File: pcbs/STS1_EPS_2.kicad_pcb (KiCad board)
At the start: 4 copper layers, 81 x 85 mm, 127 parts, among them J1 Inter-EPS, J2 Panel X+, J3 Battery Pack, J4 Panel X-, J5 Panel Y+, J6 Panel Y-, J7 Panel Z+, Q1 SI7135DP-T1-GE3, Q2 2N7002, Q3 SI7135DP-T1-GE3, Q4 2N7002, Q5 SI7135DP-T1-GE3, U1 LTC4020EUHFPBF, U10 MAX11632EEGT, U11 TMCS1101A3B-Q1, U12 BD50GA5WEFJ, U13 TMCS1101A3B-Q1, U14 LM334M, U15 LM334M, U16 LM334M, U17 LM334M, U18 LM334M, U19 TMCS1101A3B-Q1, U2 SI7272DP-T1-GE3, U20 TMCS1101A3B-Q1, U21 TMCS1101A3B-Q1, U22 TMCS1101A3B-Q1, U23 TMCS1101A3B-Q1, U24 TMCS1101A3B-Q1, U25 TMCS1101A3B-Q1, U26 TMCS1101A3B-Q1, U27 TPS2420RSAT, U3 SI7272DP-T1-GE3, U4 BQ29209DRBT, U5 MAX11632EEGT, U6 MAX11632EEGT, U7 MAX11632EEGT, U8 MAX11632EEGT, U9 MAX11632EEGT

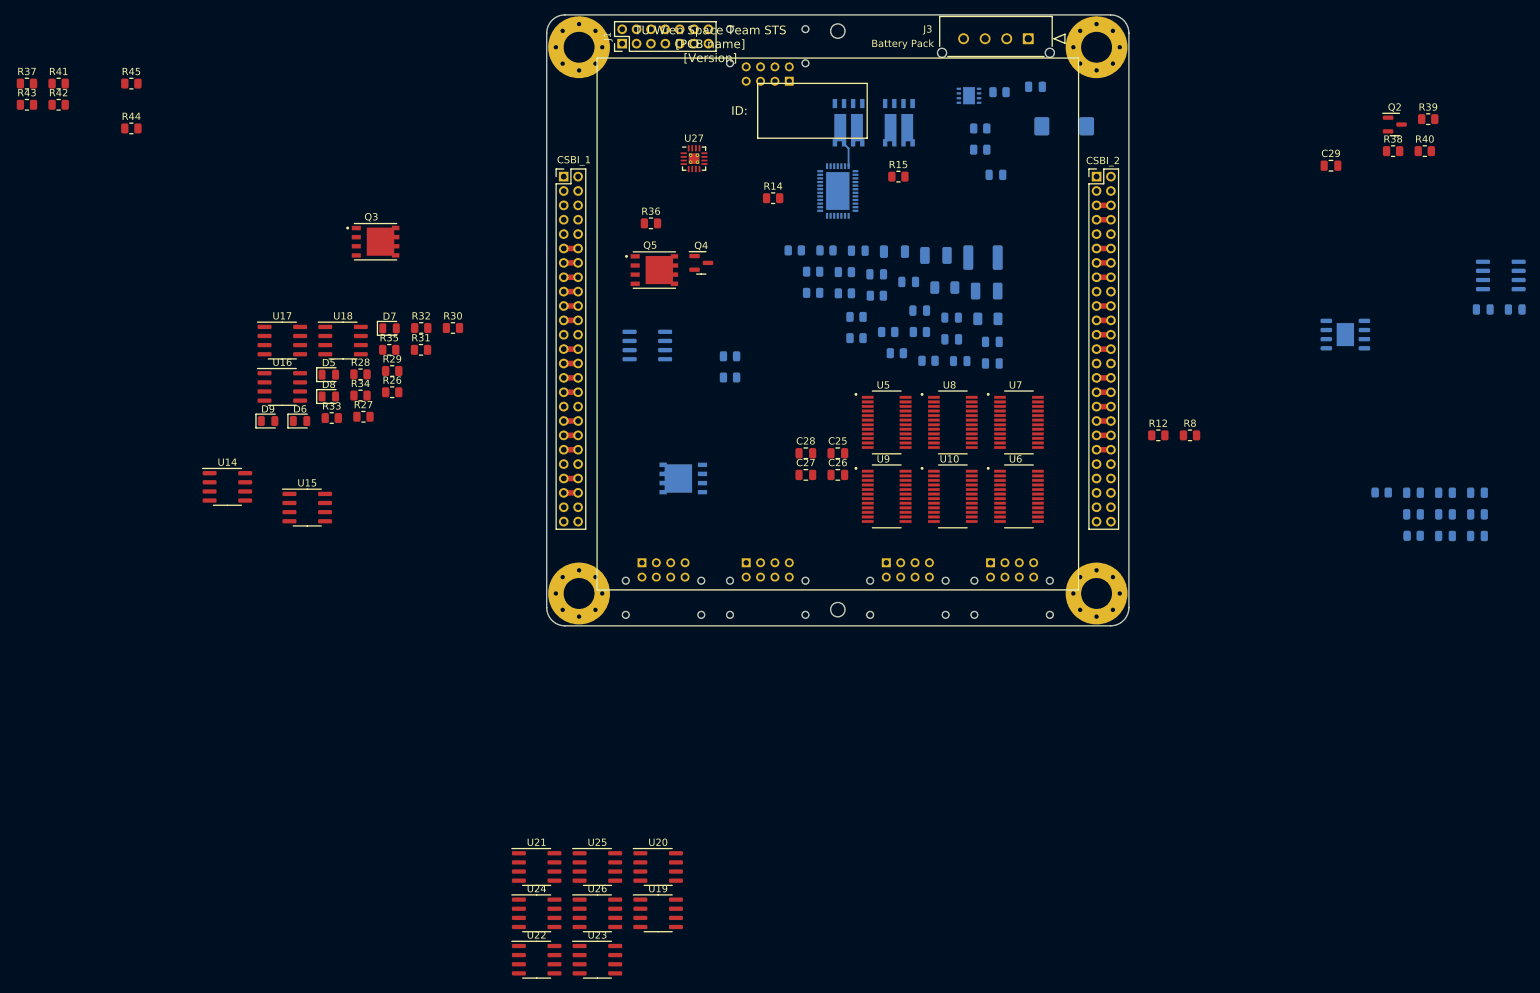
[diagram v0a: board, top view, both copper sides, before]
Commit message: Worked on STS1_EPS_1 and began work on STS1_EPS_2.
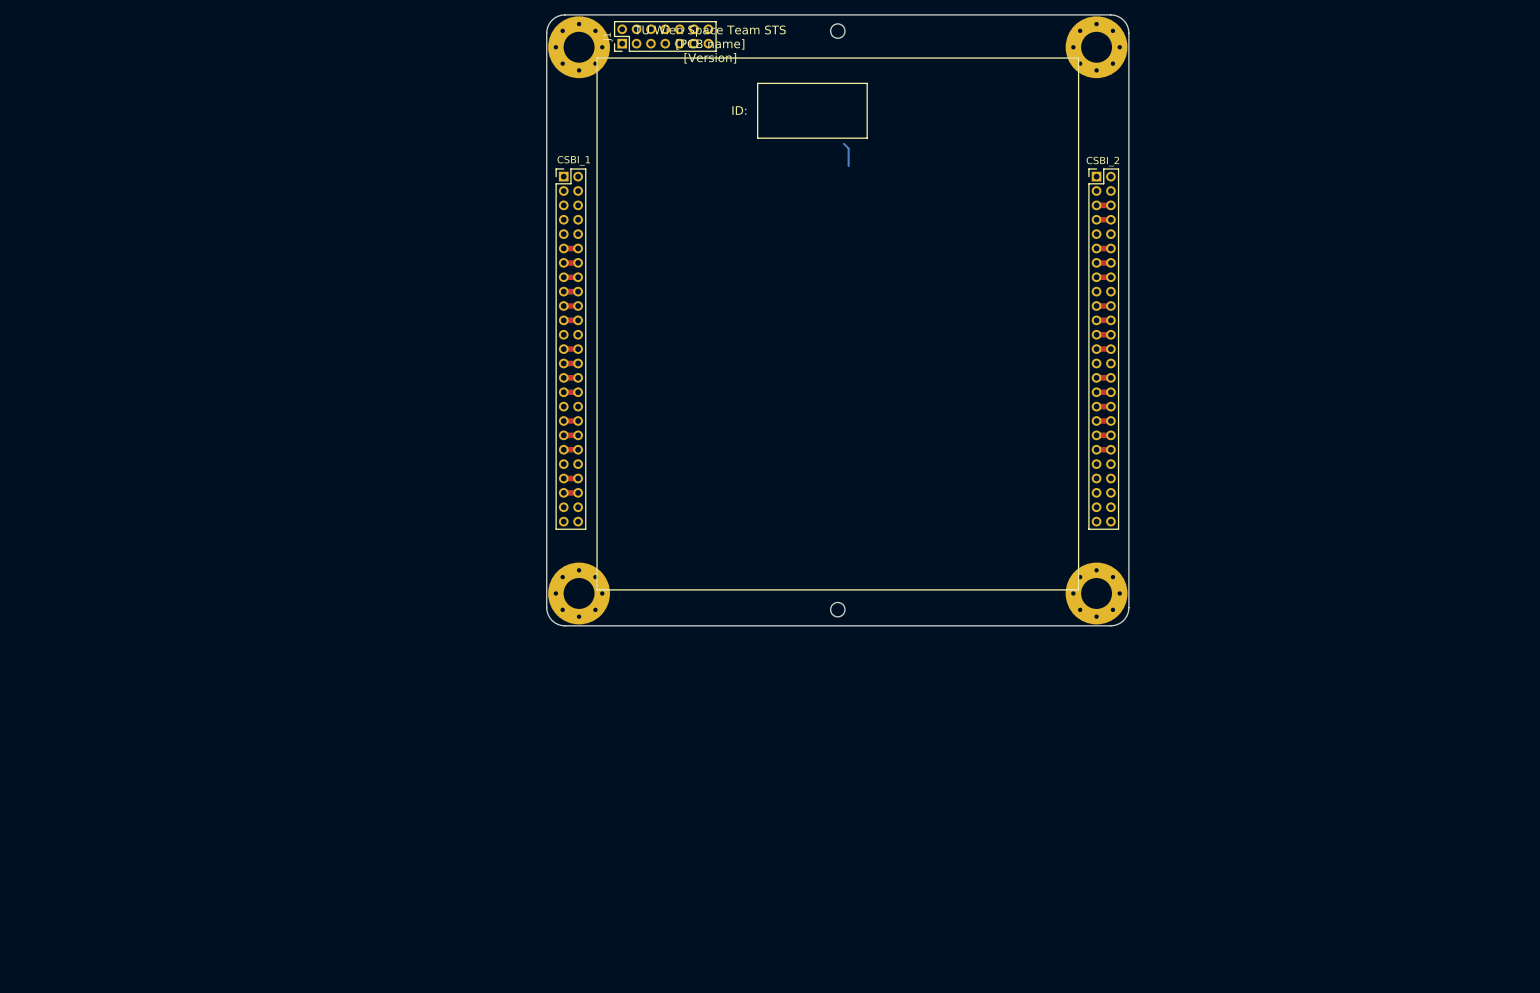
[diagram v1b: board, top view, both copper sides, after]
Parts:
- removed C1: 50u, Capacitor_Tantalum_SMD:CP_EIA-3528-12_Kemet-T
- removed C10, C9: 680p, Capacitor_SMD:C_0805_2012Metric
- removed C11: 330n, Capacitor_SMD:C_0805_2012Metric
- removed C12, C13, C17, C18, C19, C20, C21, C22, C23, C24, C25, C26, C27, C28: 100n, Capacitor_SMD:C_0805_2012Metric
- removed C14: 330u, Capacitor_Tantalum_SMD:CP_EIA-7343-43_Kemet-X
- removed C15, C16, C29: 1u, Capacitor_SMD:C_0805_2012Metric
- removed C2, C3: 1µ, Capacitor_SMD:C_0805_2012Metric
- removed C5: 220µ, Capacitor_Tantalum_SMD:CP_EIA-3528-12_Kemet-T
- removed C6: 2µ2, Capacitor_SMD:C_0805_2012Metric
- removed C7: 10µ, Capacitor_SMD:C_0805_2012Metric
- removed C8: 200n, Capacitor_SMD:C_1812_4532Metric
- removed D1, D2: SD1206T040S1R0, Diode_SMD:D_1206_3216Metric
- removed D3, D4: LED, LED_SMD:LED_0805_2012Metric
- removed D5, D6, D7, D8, D9: TS4148 RYG, Diode_SMD:D_0805_2012Metric
- removed J2: Panel X+, STS_Connector:M8085108
- removed J3: Battery Pack, STS_Connector:436500415
- removed J4: Panel X-, STS_Connector:M8085108
- removed J5: Panel Y+, STS_Connector:M8085108
- removed J6: Panel Y-, STS_Connector:M8085108
- removed J7: Panel Z+, STS_Connector:M8085108
- removed Q1, Q3, Q5: SI7135DP-T1-GE3, STS_Package_SO:POWERPAK_SO8_single
- removed Q2, Q4: 2N7002, Package_TO_SOT_SMD:SOT-23
- removed R1: 135k, Resistor_SMD:R_0805_2012Metric
- removed R10, R11: 1k, Resistor_SMD:R_0805_2012Metric
- removed R12, R2, R25, R37, R4, R41, R6, R8: 100k, Resistor_SMD:R_0805_2012Metric
- removed R13: 53k6, Resistor_SMD:R_0805_2012Metric
- removed R14, R15: 30m, Resistor_SMD:R_0805_2012Metric
- removed R16, R17, R36: R, Resistor_SMD:R_0805_2012Metric
- removed R18, R19, R21: 100, Resistor_SMD:R_0805_2012Metric
- removed R20: 17m, Resistor_SMD:R_1206_3216Metric
- removed R22, R23: 140, Resistor_SMD:R_0805_2012Metric
- removed R24: 87k5, Resistor_SMD:R_0805_2012Metric
- removed R26, R28, R30, R32, R34: 332, Resistor_SMD:R_0805_2012Metric
- removed R27, R29, R31, R33, R35: 3320, Resistor_SMD:R_0805_2012Metric
- removed R3: 180k, Resistor_SMD:R_0805_2012Metric
- removed R38: 40k2, Resistor_SMD:R_0805_2012Metric
- removed R39: 64k, Resistor_SMD:R_0805_2012Metric
- removed R40: 31k5, Resistor_SMD:R_0805_2012Metric
- removed R42, R43, R44, R45: 0, Resistor_SMD:R_0805_2012Metric
- removed R5: 31k, Resistor_SMD:R_0805_2012Metric
- removed R7: 500k, Resistor_SMD:R_0805_2012Metric
- removed R9: 166k, Resistor_SMD:R_0805_2012Metric
- removed U1: LTC4020EUHFPBF, STS_Package_DFN_QFN:AD_QFN-38_UHF
- removed U10, U5, U6, U7, U8, U9: MAX11632EEGT, STS_Package_QSOP:MAX_QSOP24
- removed U11, U13, U19, U20, U21, U22, U23, U24, U25, U26: TMCS1101A3B-Q1, Package_SO:SOIC-8_3.9x4.9mm_P1.27mm
- removed U12: BD50GA5WEFJ, Package_SO:HTSOP-8-1EP_3.9x4.9mm_P1.27mm_EP2.4x3.2mm
- removed U14, U15, U16, U17, U18: LM334M, Package_SO:SOIC-8_3.9x4.9mm_P1.27mm
- removed U2, U3: SI7272DP-T1-GE3, STS_Package_SO:POWERPAK_SO8
- removed U27: TPS2420RSAT, Package_DFN_QFN:VQFN-16-1EP_3x3mm_P0.5mm_EP1.45x1.45mm_ThermalVias
- removed U4: BQ29209DRBT, STS_Package_VSON:TI_VSON8
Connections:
- net GNDREF renamed /DS2_H
- J1 pad 11: GND -> /DS2_L
- J1 pad 9: GND -> /DS2_L
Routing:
- net /Battery Charge Controller/SW1: track 3.36 -> 0.00 mm
- net (no net): track 0.00 -> 3.36 mm
- added copper zone on In1.Cu, net /DS2_L
- removed copper zone on In1.Cu, net GND

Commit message: Finished first revision of schematic.
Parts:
- added C1: 100n, Capacitor_SMD:C_0805_2012Metric, F.Cu at (87.1, 68.8)
- added C2: 100n, Capacitor_SMD:C_0805_2012Metric, F.Cu at (223.1, 103.3)
- added C29: 1u, Capacitor_SMD:C_0805_2012Metric, F.Cu at (30.8, 111.2)
- added C3: 100n, Capacitor_SMD:C_0805_2012Metric, F.Cu at (218.7, 103.3)
- added C4: 100n, Capacitor_SMD:C_0805_2012Metric, F.Cu at (227.6, 103.3)
- added C5: 100n, Capacitor_SMD:C_0805_2012Metric, F.Cu at (238.2, 90.0)
- added F1: Fuse, Resistor_SMD:R_1206_3216Metric, F.Cu at (243.1, 83.8)
- added J2: DS1, STS_Connector:M808420245, F.Cu at (129.1, 119.4)
- added J3: DS2, STS_Connector:M808420245, F.Cu at (139.1, 119.4)
- added J4: DS3, STS_Connector:M808420245, F.Cu at (149.1, 119.4)
- added J5: DS4, STS_Connector:M808420245, F.Cu at (159.1, 119.4)
- added J6: RBF, STS_Connector:M808420245, F.Cu at (169.1, 119.4)
- added J7: Antenna Deployment, STS_Connector:M80-85104YY, F.Cu at (179.1, 54.8)
- added J8: UCI, STS_Connector:M80-85110YY, F.Cu at (155.6, 54.8)
- added Q1: 2N7002, Package_TO_SOT_SMD:SOT-23, F.Cu at (228.7, 99.6)
- added Q10: 2N7002, Package_TO_SOT_SMD:SOT-23, F.Cu at (218.9, 95.1)
- added Q11: SI7272DP-T1-GE3, STS_Package_SO:POWERPAK_SO8, F.Cu at (251.5, 100.4)
- added Q12: SI7272DP-T1-GE3, STS_Package_SO:POWERPAK_SO8, F.Cu at (251.5, 92.4)
- added Q13: 2N7002, Package_TO_SOT_SMD:SOT-23, F.Cu at (218.9, 90.7)
- added Q14: 2N7002, Package_TO_SOT_SMD:SOT-23, F.Cu at (218.9, 99.6)
- added Q15: 2N7002, Package_TO_SOT_SMD:SOT-23, F.Cu at (233.6, 90.7)
- added Q16: BSS83P, Package_TO_SOT_SMD:SOT-23, F.Cu at (233.6, 95.1)
- added Q17: 2N7002, Package_TO_SOT_SMD:SOT-23, F.Cu at (223.8, 95.1)
- added Q18: 2N7002, Package_TO_SOT_SMD:SOT-23, F.Cu at (248.2, 110.9)
- added Q19: SI7272DP-T1-GE3, STS_Package_SO:POWERPAK_SO8, F.Cu at (246.6, 75.3)
- added Q2: SI7135DP-T1-GE3, STS_Package_SO:POWERPAK_SO8_single, F.Cu at (39.6, 104.3)
- added Q20: 2N7002, Package_TO_SOT_SMD:SOT-23, F.Cu at (253.0, 110.9)
- added Q21: 2N7002, Package_TO_SOT_SMD:SOT-23, F.Cu at (248.2, 115.3)
- added Q3: SI7135DP-T1-GE3, STS_Package_SO:POWERPAK_SO8_single, F.Cu at (33.1, 100.0)
- added Q4: SI7135DP-T1-GE3, STS_Package_SO:POWERPAK_SO8_single, F.Cu at (44.9, 99.0)
- added Q5: SI7135DP-T1-GE3, STS_Package_SO:POWERPAK_SO8_single, F.Cu at (33.1, 106.5)
- added Q6: 2N7002, Package_TO_SOT_SMD:SOT-23, F.Cu at (223.8, 90.7)
- added Q7: 2N7002, Package_TO_SOT_SMD:SOT-23, F.Cu at (223.8, 99.6)
- added Q8: BSS83P, Package_TO_SOT_SMD:SOT-23, F.Cu at (228.7, 90.7)
- added Q9: 2N7002, Package_TO_SOT_SMD:SOT-23, F.Cu at (228.7, 95.1)
- added R1: 0, Resistor_SMD:R_0805_2012Metric, F.Cu at (43.8, 108.0)
- added R10: 100k, Resistor_SMD:R_0805_2012Metric, F.Cu at (279.3, 89.9)
- added R11: 0, Resistor_SMD:R_0805_2012Metric, F.Cu at (274.9, 95.8)
- added R12: 100k, Resistor_SMD:R_0805_2012Metric, F.Cu at (256.7, 119.0)
- added R13: 100k, Resistor_SMD:R_0805_2012Metric, F.Cu at (257.2, 116.0)
- added R14: 100k, Resistor_SMD:R_0805_2012Metric, F.Cu at (262.1, 113.1)
- added R15: 100k, Resistor_SMD:R_0805_2012Metric, F.Cu at (261.6, 116.0)
- added R16: 100k, Resistor_SMD:R_0805_2012Metric, F.Cu at (257.7, 110.1)
- added R17: 1M, Resistor_SMD:R_0805_2012Metric, F.Cu at (257.7, 113.1)
- added R18: 887k, Resistor_SMD:R_0805_2012Metric, F.Cu at (252.8, 114.6)
- added R19: 127k, Resistor_SMD:R_0805_2012Metric, F.Cu at (262.1, 110.1)
- added R2: 100k, Resistor_SMD:R_0805_2012Metric, F.Cu at (232.0, 103.3)
- added R20: 127k, Resistor_SMD:R_0805_2012Metric, F.Cu at (261.1, 119.0)
- added R21: 127k, Resistor_SMD:R_0805_2012Metric, F.Cu at (247.9, 119.0)
- added R22: 187k, Resistor_SMD:R_0805_2012Metric, F.Cu at (270.2, 117.1)
- added R23: 787k, Resistor_SMD:R_0805_2012Metric, F.Cu at (275.0, 110.1)
- added R24: 10k, Resistor_SMD:R_0805_2012Metric, F.Cu at (270.2, 114.2)
- added R25: 470k, Resistor_SMD:R_0805_2012Metric, F.Cu at (243.8, 8.78)
- added R3: 100k, Resistor_SMD:R_0805_2012Metric, F.Cu at (238.2, 92.9)
- added R37: 100k, Resistor_SMD:R_0805_2012Metric, F.Cu at (39.4, 108.0)
- added R38: 40k2, Resistor_SMD:R_0805_2012Metric, F.Cu at (35.2, 111.2)
- added R39: 64k, Resistor_SMD:R_0805_2012Metric, F.Cu at (44.3, 103.5)
- added R4: 100k, Resistor_SMD:R_0805_2012Metric, F.Cu at (233.3, 98.8)
- added R40: 31k5, Resistor_SMD:R_0805_2012Metric, F.Cu at (49.6, 98.2)
- added R41: 100k, Resistor_SMD:R_0805_2012Metric, F.Cu at (39.6, 110.9)
- added R42: 0, Resistor_SMD:R_0805_2012Metric, F.Cu at (54.0, 98.2)
- added R5: 100k, Resistor_SMD:R_0805_2012Metric, F.Cu at (238.2, 95.9)
- added R6: 100k, Resistor_SMD:R_0805_2012Metric, F.Cu at (252.3, 119.0)
- added R7: 100k, Resistor_SMD:R_0805_2012Metric, F.Cu at (242.7, 89.9)
- added R8: 100k, Resistor_SMD:R_0805_2012Metric, F.Cu at (274.9, 89.9)
- added R9: 0, Resistor_SMD:R_0805_2012Metric, F.Cu at (274.9, 92.9)
- added U1: LTC6995IDCB-1, Package_DFN_QFN:DFN-6-1EP_3x2mm_P0.5mm_EP1.65x1.35mm, F.Cu at (87.5, 65.5)
- added U2: 4072, Package_SO:SOIC-14_3.9x8.7mm_P1.27mm, F.Cu at (227.1, 69.3)
- added U27: TPS2420RSAT, Package_DFN_QFN:VQFN-16-1EP_3x3mm_P0.5mm_EP1.45x1.45mm_ThermalVias, F.Cu at (39.8, 99.4)
- added U3: MIC841, Package_DFN_QFN:TDFN-6-1EP_2.5x2.5mm_P0.65mm_EP1.3x2mm, F.Cu at (163.1, 68.3)
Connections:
- net /Analog Digital Converters/COBC_SPI_1 renamed /CSBI/COBC_SPI_1
- net /Analog Digital Converters/COBC_SPI_2 renamed /CSBI/COBC_SPI_2
- net /Analog Digital Converters/COBC_SPI_3 renamed /CSBI/COBC_SPI_3
- net /Analog Digital Converters/COBC_SPI_4 renamed /CSBI/COBC_SPI_4
- net /Analog Digital Converters/COBC_SPI_5 renamed /CSBI/COBC_SPI_5
- net /Analog Digital Converters/COBC_SPI_6 renamed /CSBI/COBC_SPI_6
- net /Analog Digital Converters/EDU_SPI_1 renamed /CSBI/EDU_SPI_1
- net /Analog Digital Converters/EDU_SPI_2 renamed /CSBI/EDU_SPI_2
- net /Analog Digital Converters/EDU_SPI_3 renamed /CSBI/EDU_SPI_3
- net /Analog Digital Converters/EDU_SPI_4 renamed /CSBI/EDU_SPI_4
- net /Analog Digital Converters/EDU_SPI_5 renamed /CSBI/EDU_SPI_5
- net /Analog Digital Converters/EDU_SPI_6 renamed /CSBI/EDU_SPI_6
- net /BAT_FAULT renamed /EPS_BAT_FAULT
- net /BAT_GOOD renamed /EPS_BAT_GOOD
- net /Cubesat Bus Interface/UART_COBC_EDU_1 renamed /CSBI/UART_COBC_EDU_1
- net /Cubesat Bus Interface/UART_COBC_EDU_2 renamed /CSBI/UART_COBC_EDU_2
- net /Cubesat Bus Interface/UCI_COBC_UART_1 renamed /CSBI/UCI_COBC_UART_1
- net /Cubesat Bus Interface/UCI_COBC_UART_2 renamed /CSBI/UCI_COBC_UART_2
- CSBI_2 pad 23: unconnected-(CSBI_2-Pad23) -> /EPS_ANT_DEPLOY
- CSBI_2 pad 25: /BAT_CHARGING -> unconnected-(CSBI_2-Pad25)
- CSBI_2 pad 26: /BAT_CHARGING -> unconnected-(CSBI_2-Pad25)
- J1 pad 1: /DS1_H -> /INTERNAL_V
- J1 pad 10: /DS3_H -> /DS2_SIGNAL_1
- J1 pad 11: /DS2_L -> GND
- J1 pad 12: /DS4_L -> GND
- J1 pad 13: /DS3_H -> GND
- J1 pad 14: /DS4_L -> GND
- J1 pad 3: /DS1_L -> /INTERNAL_V
- J1 pad 5: /DS2_H -> /INTERNAL_V
- J1 pad 6: /DT_SIGNAL -> /BATT_RAW
- J1 pad 7: /DS2_H -> /INTERNAL_V
- J1 pad 8: /RBF_SIGNAL -> /VOUT_I
- J1 pad 9: /DS2_L -> /DS1_SIGNAL_1
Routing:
- net unconnected-(CSBI_2-Pad25): track 0.00 -> 2.00 mm
- net unconnected-(CSBI_2-Pad24): track 2.00 -> 0.00 mm
- net /EPS_ANT_DEPLOY: track 0.00 -> 2.00 mm
- net /BAT_CHARGING: track 2.00 -> 0.00 mm
- added copper zone on In1.Cu, net GND
- removed copper zone on In1.Cu, net /DS2_L
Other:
- outline, holes or cut-outs redrawn
- board text added: "TU Wien Space Team STS STS1_EPS_2 1.0"
- board text removed: "TU Wien Space Team STS [PCB name] [Version]"

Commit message: Worked on STS1_EPS_2 layout.
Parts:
- moved U3 45.4 mm to (208.4, 65.8)
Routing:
- net (no net): track 3.36 -> 0.00 mm

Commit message: EPS_2 Layout nearly finished, alot DRC Errors
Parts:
- moved Q3 138.4 mm to (169.3, 75.5), turned to 90 degrees
- moved R11 137.2 mm to (138.9, 77.4), turned to 90 degrees
- moved R10 135.7 mm to (143.9, 80.6)
- moved R37 134.0 mm to (170.6, 80.6)
- moved Q5 131.0 mm to (160.4, 75.5), turned to 90 degrees
- moved R9 128.0 mm to (147.7, 77.4), turned to 90 degrees
- moved R23 127.5 mm to (157.9, 59.5), turned to 90 degrees
- moved R6 126.4 mm to (126.2, 111.6), turned to 90 degrees
- moved R41 125.8 mm to (161.7, 80.6)
- moved R24 123.2 mm to (157.9, 63.3), turned to 90 degrees
- moved R22 122.9 mm to (157.9, 67.2), turned to 90 degrees
- moved R8 122.4 mm to (152.8, 80.6)
- moved R12 120.6 mm to (136.3, 111.6), turned to 90 degrees
- moved R15 118.5 mm to (147.1, 85.6)
- moved R1 116.9 mm to (156.6, 77.4), turned to 90 degrees
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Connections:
- J1 pad 12: GND -> /DS4_SIGNAL_1
- J1 pad 13: GND -> /BATT_RAW
- J1 pad 14: GND -> /BATT_RAW
- J1 pad 4: /BATT_RAW -> GND
- J1 pad 6: /BATT_RAW -> GND
- Q18 pad 1: /DS4_SIGNAL_1 -> /DS4_SIGNAL_2
- R14 pad 1: /DS4_SIGNAL_1 -> /DS4_SIGNAL_2
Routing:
- net /+5V: track 0.00 -> 265.3 mm, vias 0 -> 11
- net /Bus Gate/VOUT_GATED: track 0.00 -> 124.2 mm, vias 0 -> 4
- net GND: track 0.00 -> 116.5 mm, vias 0 -> 14
- net /DS4_SIGNAL_1: track 0.00 -> 88.1 mm, vias 0 -> 2
- net /DS2_SIGNAL_1: track 0.00 -> 66.8 mm, vias 0 -> 2
- net /DS1_SIGNAL_1: track 0.00 -> 63.4 mm
- net /RBF_SIGNAL_2: track 0.00 -> 58.3 mm, vias 0 -> 2
- net Net-(Q3-Pad1): track 0.00 -> 54.0 mm, vias 0 -> 2
- net /EPS_BAT_GOOD: track 2.00 -> 52.8 mm, vias 0 -> 2
- net /DS3_SIGNAL_1: track 0.00 -> 41.1 mm, vias 0 -> 2
- net Net-(U1-Pad1): track 0.00 -> 36.7 mm, vias 0 -> 2
- net /DS2_SIGNAL_2: track 0.00 -> 36.3 mm, vias 0 -> 2
- net /INTERNAL_V: track 0.00 -> 35.8 mm
- net /RBF_SIGNAL_1: track 0.00 -> 33.9 mm
- net /DS1_SIGNAL_2: track 0.00 -> 33.2 mm, vias 0 -> 3
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
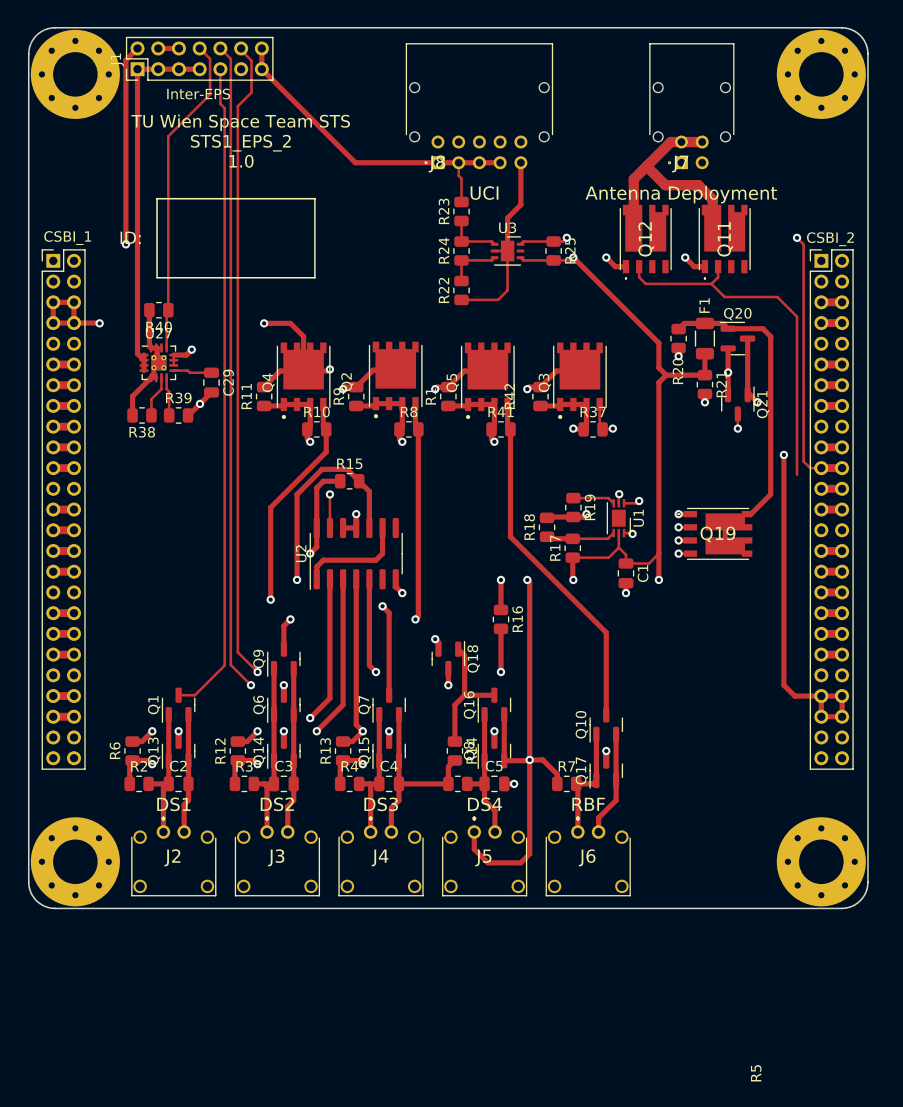
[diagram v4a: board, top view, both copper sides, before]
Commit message: EPS_2 removes some DRC errors, added Areas
sry for bad commit messages
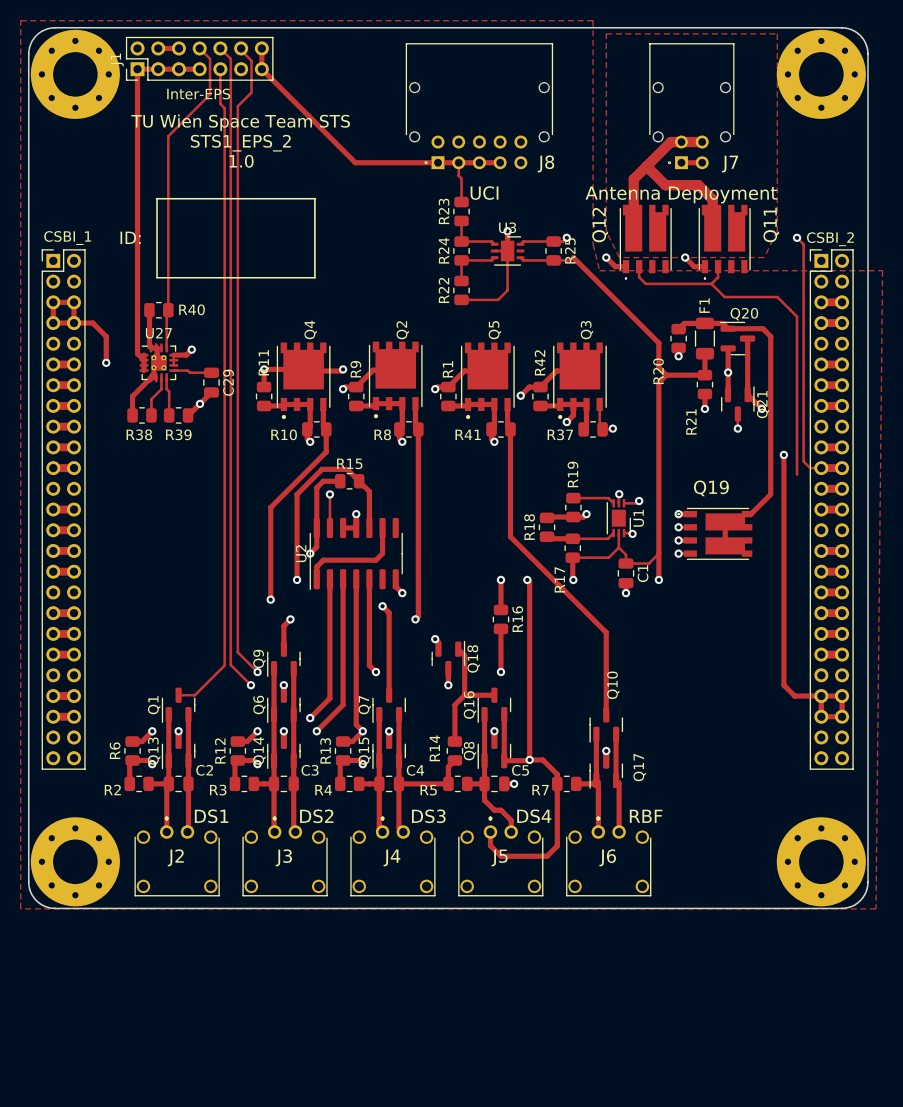
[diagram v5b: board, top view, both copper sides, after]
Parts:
- moved J6 1.98 mm to (171.1, 119.4)
- moved J5 1.56 mm to (160.7, 119.4)
- moved J4 1.15 mm to (150.3, 119.4)
- moved J3 0.74 mm to (139.9, 119.4)
- moved J2 0.32 mm to (129.5, 119.4)
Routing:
- net /+5V: track 265.3 -> 199.9 mm, vias 11 -> 9
- net GND: track 116.5 -> 108.3 mm, vias 14 -> 15
- net /DS2_SIGNAL_3: track 21.5 -> 24.7 mm
- net /BAT_RAW: track 0.00 -> 2.00 mm
- net Net-(Q20-Pad3): track 12.6 -> 14.3 mm
- net /Deployment Switches + RBF/DS4-: track 13.4 -> 14.4 mm
- net /Bus Gate/VOUT_GATED: track 124.2 -> 123.4 mm
- net /Deployment Switches + RBF/RBF+: track 11.2 -> 11.8 mm
- added copper zone on F.Cu, net /+5V
- added copper zone on In2.Cu, net /+5V
- added copper zone on F.Cu, net /Antenna Deployment/ANT_DEPLOY-
- added copper zone on In2.Cu, net /Bus Gate/VOUT_GATED
